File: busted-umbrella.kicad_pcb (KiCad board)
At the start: 4 copper layers, 50 x 50 mm, 45 parts, among them J1 SWD, J2 DB9_Male, M1 USB_B, SW1 TL2201, U1 ATSAME51J18A-MF, U2 LM3940IMP-3.3_SOT223, U3 CRV2S0505SC, U4 ADM3058E, Y1 8MHz

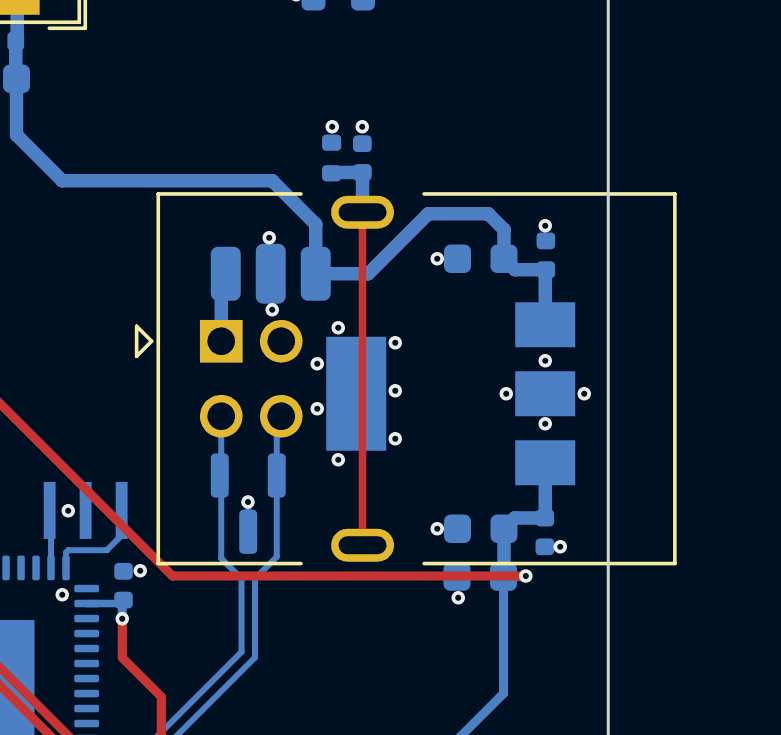
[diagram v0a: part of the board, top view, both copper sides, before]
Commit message: changed ldo
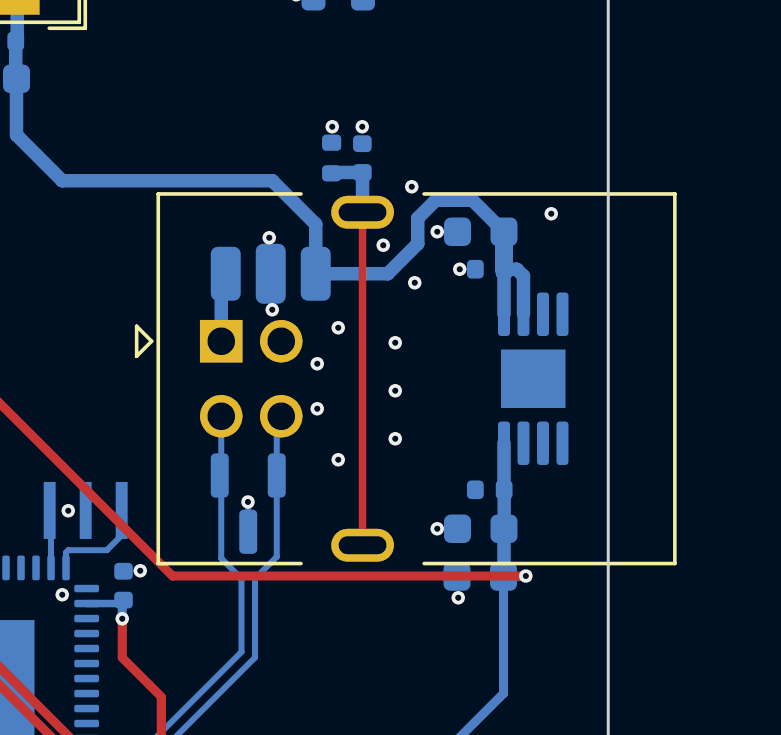
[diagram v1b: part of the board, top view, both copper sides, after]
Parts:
- U2: value LM3940IMP-3.3_SOT223 -> TPS7B82-Q1; footprint Package_TO_SOT_SMD:SOT-223-3_TabPin2 -> Package_SO:MSOP-8-1EP_3x3mm_P0.65mm_EP1.95x2.15mm
- moved U2 2.80 mm to (47.5, 25.0), turned to -90 degrees
- moved C15 2.32 mm to (46.0, 28.7), turned to 180 degrees
- moved C14 1.93 mm to (46.0, 21.4), turned to 180 degrees
- moved C13 0.90 mm to (45.8, 20.1)
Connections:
- U2 pad 2: GND -> +5V
- U2 pad 3: +3V3 -> GND
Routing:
- net +5V: track 29.6 -> 30.9 mm
- net +3V3: track 125.3 -> 124.7 mm
- net GND: vias 48 -> 47
